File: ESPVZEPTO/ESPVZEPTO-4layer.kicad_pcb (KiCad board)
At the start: 4 copper layers, 12 x 16.8 mm, 22 parts, among them J1 USB_A, J2 Conn_02x05_Odd_Even, U1 AP7333-33SRG-7, U2 ESP32-C3, Y1 Crystal_GND24_Small

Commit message: tweeks
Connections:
- U2 pad 10: Net-(U2-Pad10) -> GND
- U2 pad 12: Net-(U2-Pad12) -> GND
- U2 pad 13: Net-(U2-Pad13) -> GND

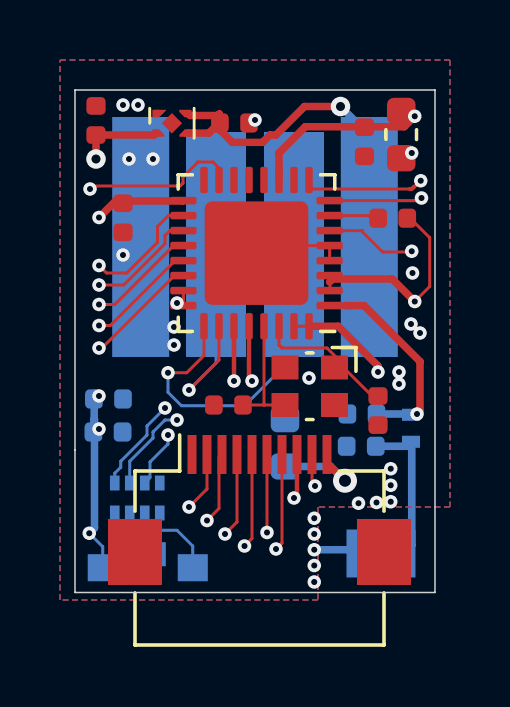
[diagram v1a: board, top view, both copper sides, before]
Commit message: small tweeks and update to pin strapping
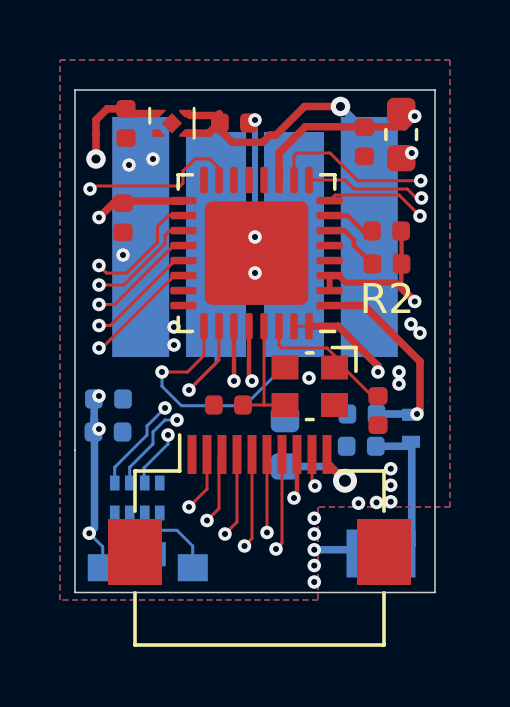
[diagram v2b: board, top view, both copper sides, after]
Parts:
- added R2: R_Small, Resistor_SMD:R_0402_1005Metric, F.Cu at (151.9, 42.8)
- AE1: value Antenna -> Antenna_Shield
- C2, C3: value C_Small -> 10pF
- J2: value Conn_02x05_Odd_Even -> Conn_01x10_MountingPin
- U1: value AP7333-33SRG-7 -> NCP115AMX330TCG
- Y1: value Crystal_GND24_Small -> 40Mhz
- moved C4 1.00 mm to (143.2, 38.1), turned to 270 degrees
- moved R1 0.47 mm to (151.9, 41.7)
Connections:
- J2 pad MP: (no net) -> GND
- RN1 pad 4: Net-(RN1-Pad4) -> (no net)
- RN1 pad 5: Net-(RN1-Pad5) -> (no net)
- U1 pad 1: GND -> +3V3
- U1 pad 2: +3V3 -> GND
- U2 pad 10: GND -> /LED_R
- U2 pad 12: GND -> (no net)
- U2 pad 13: GND -> (no net)
- U2 pad 14: Net-(U2-Pad14) -> (no net)
- U2 pad 16: /GP10 -> (no net)
- U2 pad 4: GND -> (no net)
- U2 pad 5: GND -> (no net)
- U2 pad 6: /LED_B -> Net-(R2-Pad2)
- U2 pad 8: /LED_G -> /LED_B
- U2 pad 9: /LED_R -> /LED_G
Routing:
- net Net-(R2-Pad2): track 0.00 -> 2.00 mm
- net /LED_G: track 19.3 -> 20.6 mm
- net /LED_B: track 17.7 -> 18.8 mm
- net /LED_R: track 21.4 -> 22.3 mm
- net GND: track 6.84 -> 6.63 mm, vias 26 -> 24
